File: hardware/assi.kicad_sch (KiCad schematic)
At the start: 16 parts, among them Q5 PMV450ENEA

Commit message: Add the Cube project
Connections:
- net IN_BUZZ renamed IN_BUZZER
- net OUT_BUZZ renamed OUT_BUZZER
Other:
- moved on the sheet: Q5, R?

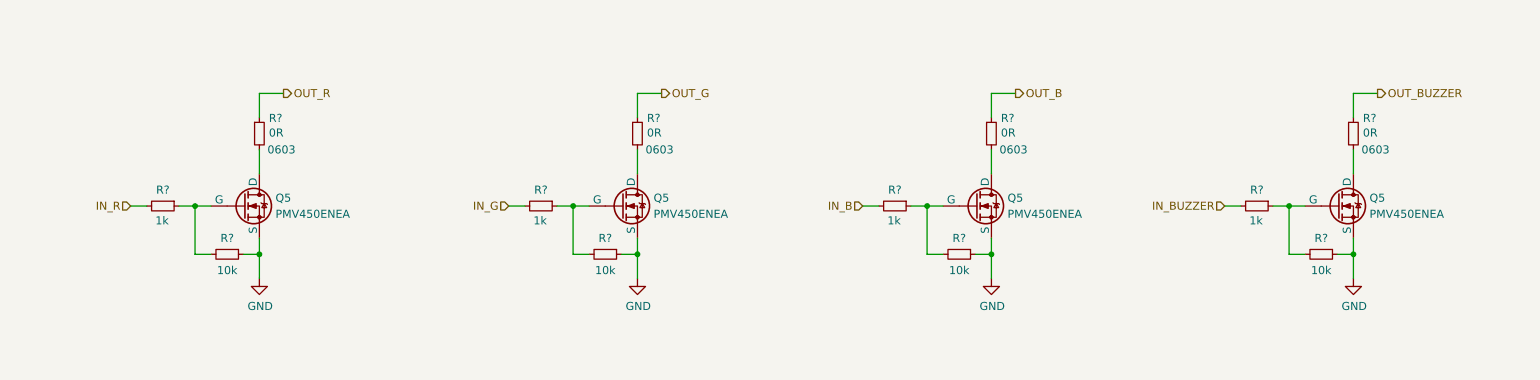
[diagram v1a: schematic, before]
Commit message: Improve the schematic
- add anti-aliasing filters
- rearrange the main connector signals
- improve the power filtering
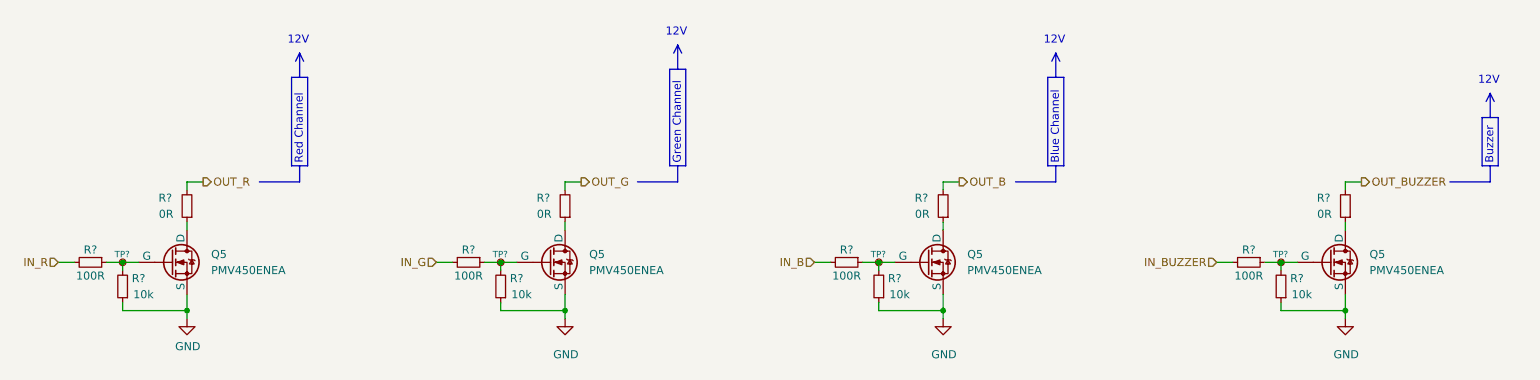
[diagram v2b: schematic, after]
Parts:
- removed Q5 (x4): PMV450ENEA, symbol Simulation_SPICE:NMOS
- removed R? (x4): 0R, Resistor_SMD:R_0603_1608Metric, symbol Device:R_Small
- removed R? (x4): 1k, Resistor_SMD:R_0402_1005Metric, symbol Device:R_Small
- removed R? (x4): 10k, Resistor_SMD:R_0402_1005Metric, symbol Device:R_Small
- added Q5 (x4): PMV450ENEA, symbol Simulation_SPICE:NMOS
- added R? (x4): 10k, Resistor_SMD:R_0603_1608Metric, symbol Device:R_Small
- added R? (x4): 100R, Resistor_SMD:R_0603_1608Metric, symbol Device:R_Small
- added R? (x4): 0R, Resistor_SMD:R_0603_1608Metric, symbol Device:R_Small
- added TP? (x4): TestPoint_Small, TestPoint:TestPoint_Pad_D1.0mm, symbol Connector:TestPoint_Small
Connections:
- net GND: now also Q5.3 (S), Q5.3 (S), Q5.3 (S), Q5.3 (S), R?.1, R?.1, R?.1, R?.1
- net IN_B: now also R?.2
- net IN_BUZZER: now also R?.2
- net IN_G: now also R?.2
- net IN_R: now also R?.2
- net OUT_B: now also R?.2
- net OUT_BUZZER: now also R?.2
- net OUT_G: now also R?.2
- net OUT_R: now also R?.2
- new net: Q5.1 (D), R?.1 (x4)
- new net: Q5.2 (G), R?.1, R?.2, TP?.1 (x4)
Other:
- note added: "12V"
- note added: "Blue Channel"
- note added: "Buzzer"
- note added: "Green Channel"
- note added: "Red Channel"

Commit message: Set component values
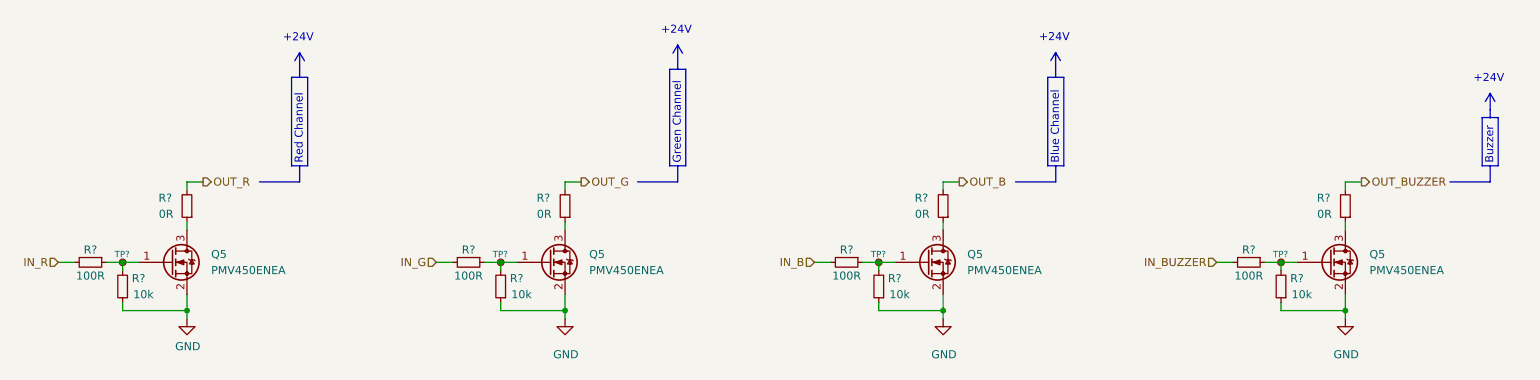
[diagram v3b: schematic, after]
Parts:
- Q5: symbol Simulation_SPICE:NMOS -> Device:Q_NMOS_GSD
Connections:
- net GND: now also Q5.2 (S), Q5.2 (S), Q5.2 (S), Q5.2 (S); no longer Q5.3 (S), Q5.3 (S), Q5.3 (S), Q5.3 (S)
- net at Q5.1 (G): now also R?.1, R?.2, TP?.1; no longer R?.1
- net at R?.1, R?.2, TP?.1: now also Q5.1 (G); no longer Q5.2 (G) (x3)
- net at R?.1: now also Q5.3 (D); no longer Q5.1 (D) (x3)
- new net: Q5.3 (D), R?.1
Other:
- note added: "+24V"
- note removed: "12V"

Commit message: Improve the schematic according to the feedback
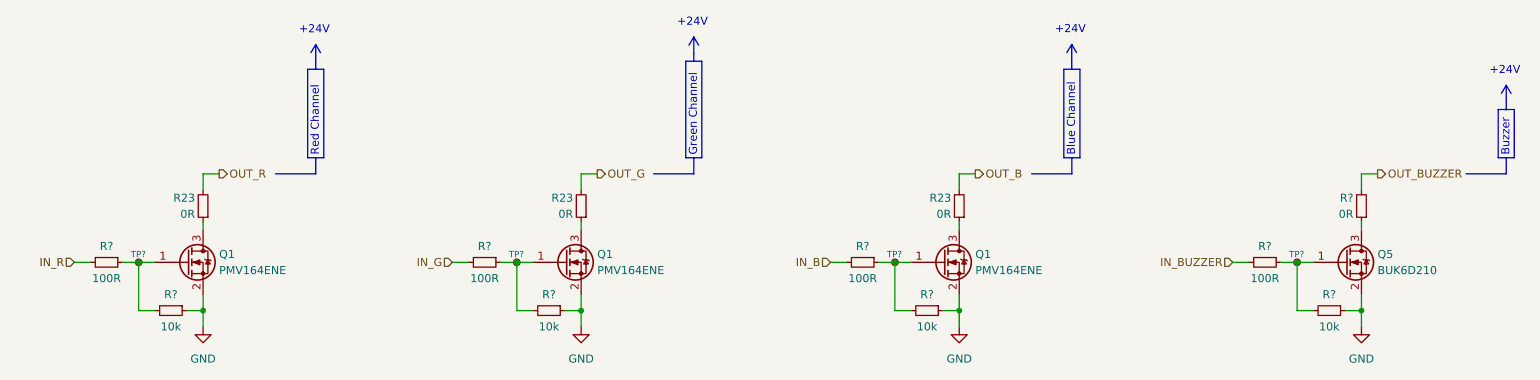
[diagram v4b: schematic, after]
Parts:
- removed Q5 (x4): PMV450ENEA, symbol Device:Q_NMOS_GSD
- removed R? (x4): 10k, Resistor_SMD:R_0603_1608Metric, symbol Device:R_Small
- removed R? (x4): 100R, Resistor_SMD:R_0603_1608Metric, symbol Device:R_Small
- removed R? (x4): 0R, Resistor_SMD:R_0603_1608Metric, symbol Device:R_Small
- removed TP? (x4): TestPoint_Small, TestPoint:TestPoint_Pad_D1.0mm, symbol Connector:TestPoint_Small
- added Q1 (x3): PMV164ENE, Package_TO_SOT_SMD:SOT-23, symbol Device:Q_NMOS_GSD
- added Q5: BUK6D210, Package_DFN_QFN:Diodes_UDFN2020-6_Type-F, symbol Device:Q_NMOS_GSD
- added R23 (x3), R?: 0R, Resistor_SMD:R_0603_1608Metric, symbol Device:R_Small
- added R? (x4): 10k, Resistor_SMD:R_0603_1608Metric, symbol Device:R_Small
- added R? (x4): 100R, Resistor_SMD:R_0603_1608Metric, symbol Device:R_Small
- added TP? (x4): TestPoint_Small, TestPoint:TestPoint_Pad_D1.0mm, symbol Connector:TestPoint_Small
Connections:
- net GND: now also Q1.2 (S), Q1.2 (S), Q1.2 (S), Q5.2 (S), R?.1, R?.1, R?.1, R?.1
- net IN_B: now also R?.2
- net IN_BUZZER: now also R?.2
- net IN_G: now also R?.2
- net IN_R: now also R?.2
- net OUT_B: now also R23.2
- net OUT_BUZZER: now also R?.2
- net OUT_G: now also R23.2
- net OUT_R: now also R23.2
- new net: Q1.1 (G), R?.1, R?.2, TP?.1 (x3)
- new net: Q1.3 (D), R23.1 (x3)
- new net: Q5.1 (G), R?.1, R?.2, TP?.1
- new net: Q5.3 (D), R?.1
